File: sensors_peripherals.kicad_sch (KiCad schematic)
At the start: 17 parts, among them J2 Conn_01x14, J4 Micro_SD_Card_Det1, J5 Conn_01x14, J6 Conn_01x02, U3 W25Q128JVS, U6 ICM-42688-P

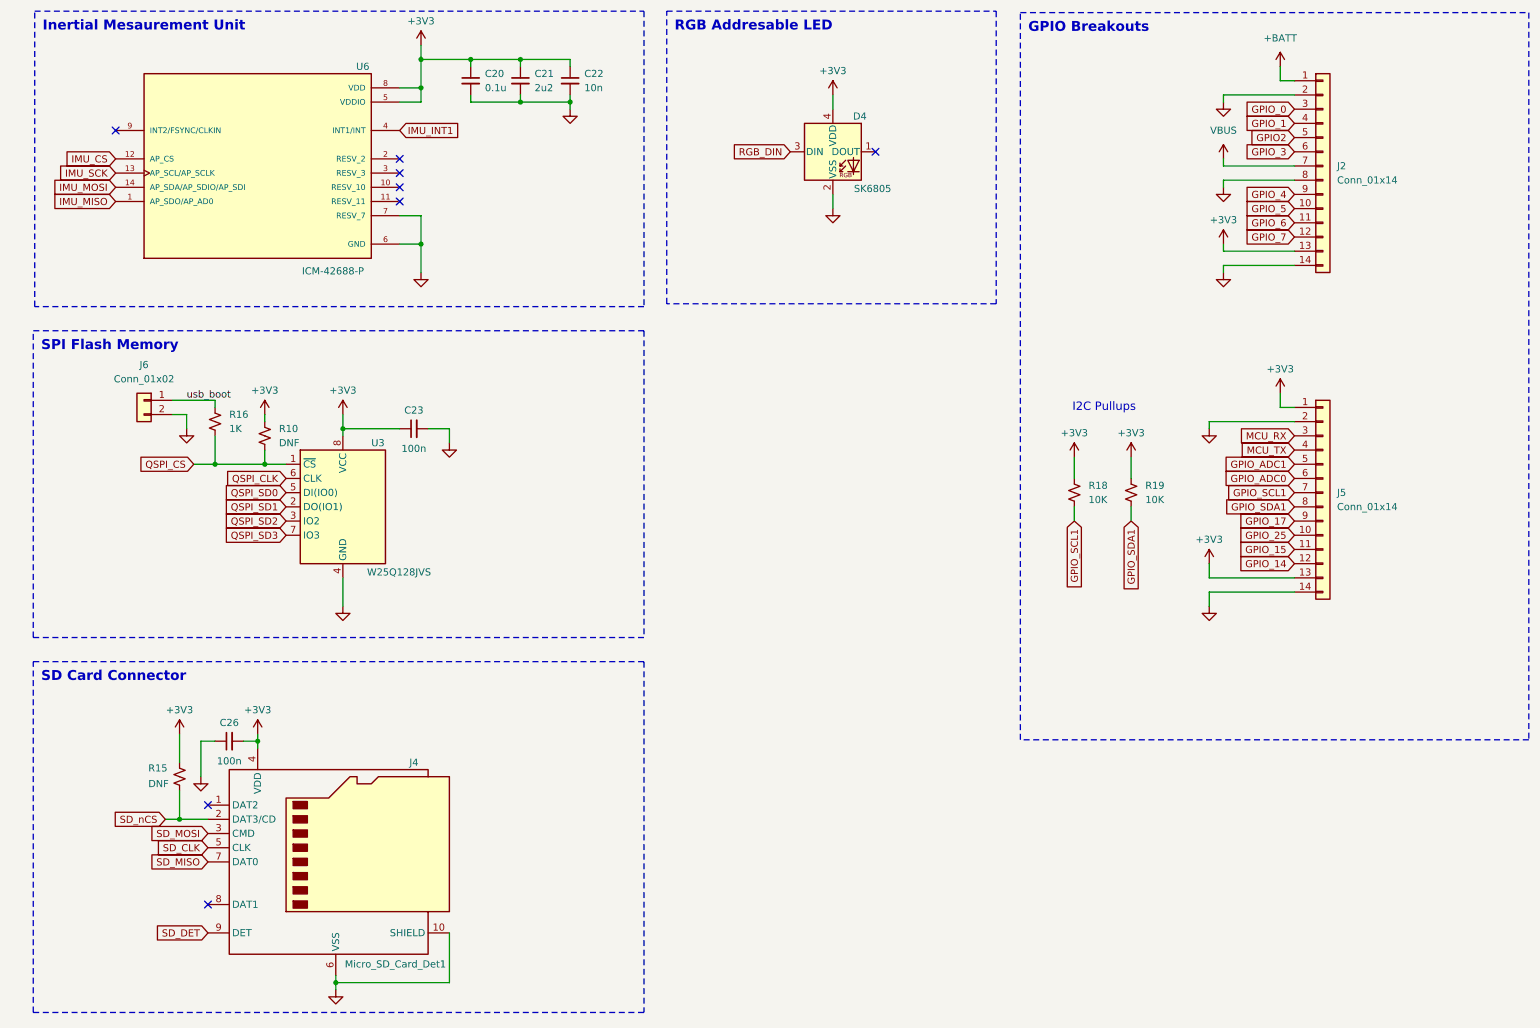
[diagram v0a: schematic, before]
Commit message: Added a bootloader button and made some other QOL changes... mostly aesthetic.
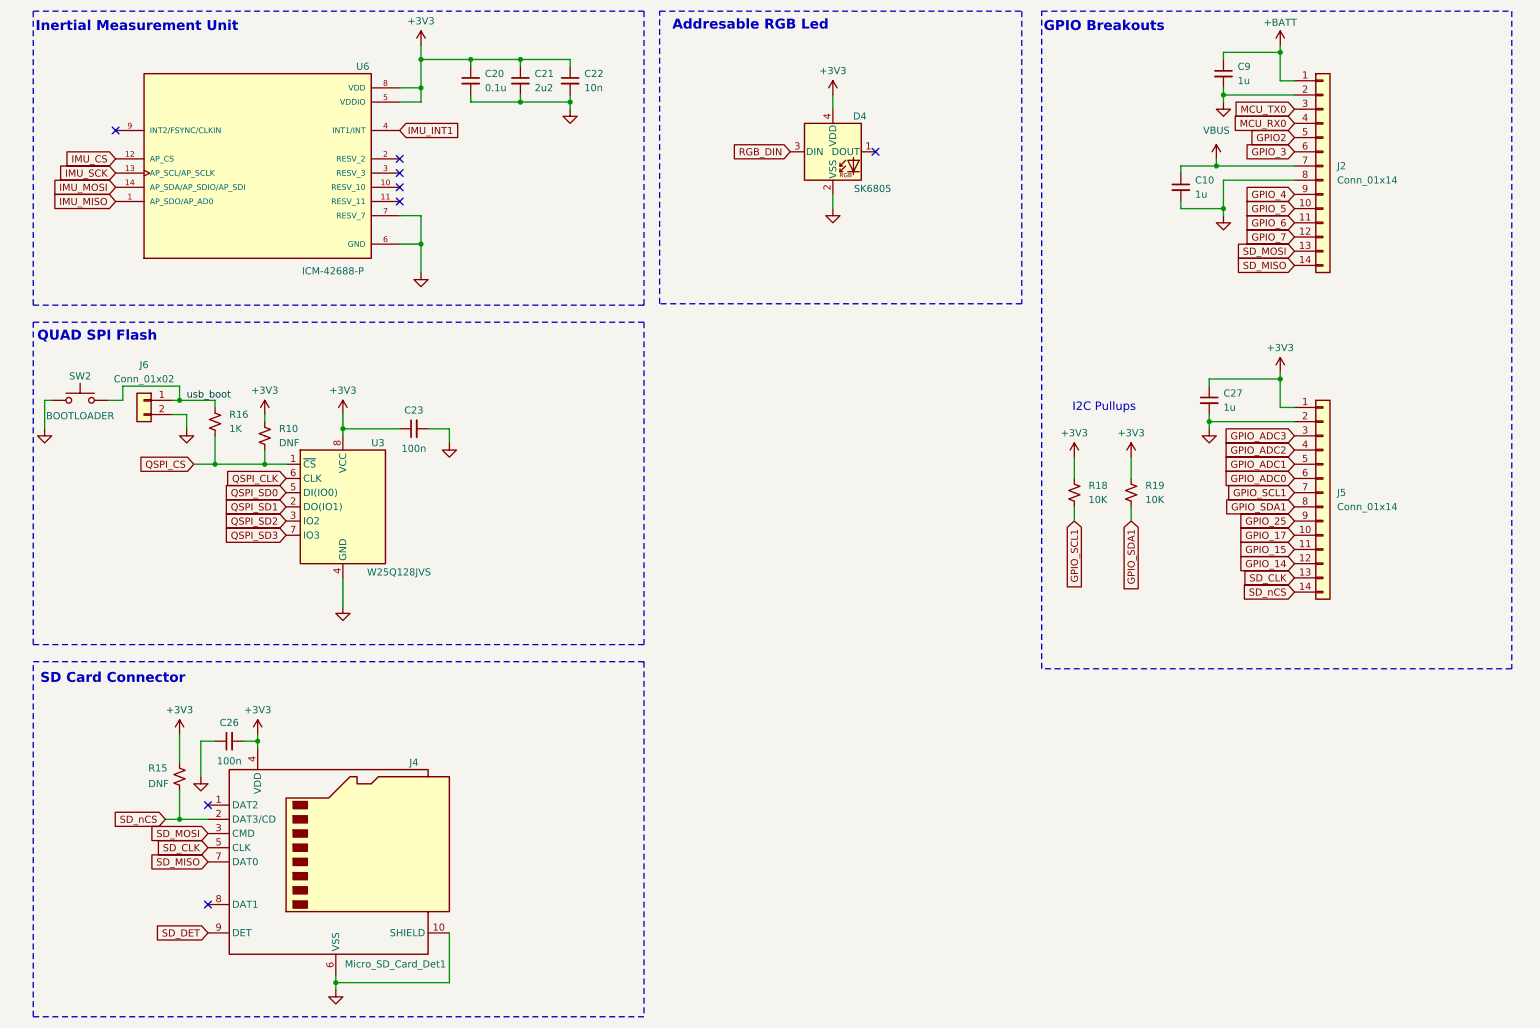
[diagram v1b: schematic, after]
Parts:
- added C10, C27, C9: 1u, Capacitor_SMD:C_0402_1005Metric, symbol Device:C_Small
- added SW2: BOOTLOADER, Button_Switch_SMD:SW_SPST_PTS647_Sx38, symbol Switch:SW_Push
- C26: footprint Capacitor_SMD:C_0201_0603Metric -> Capacitor_SMD:C_0805_2012Metric_Pad1.18x1.45mm_HandSolder
- R15: footprint Resistor_SMD:R_0805_2012Metric -> Resistor_SMD:R_0805_2012Metric_Pad1.20x1.40mm_HandSolder
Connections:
- net +3V3: now also C27.1; no longer J2.13 (Pin_13), J5.13 (Pin_13)
- net +BATT: now also C9.1
- net GND: now also C10.2, C27.2, C9.2, SW2.1; no longer J2.14 (Pin_14), J5.14 (Pin_14)
- net GPIO_17: now also J5.10 (Pin_10); no longer J5.9 (Pin_9)
- net GPIO_25: now also J5.9 (Pin_9); no longer J5.10 (Pin_10)
- net SD_CLK: now also J5.13 (Pin_13)
- net SD_MISO: now also J2.14 (Pin_14)
- net SD_MOSI: now also J2.13 (Pin_13)
- net SD_nCS: now also J5.14 (Pin_14)
- net VBUS: now also C10.1
- net usb_boot: now also SW2.2
- net GPIO_0 renamed MCU_TX0
- net GPIO_1 renamed MCU_RX0
- net MCU_RX renamed GPIO_ADC3
- net MCU_TX renamed GPIO_ADC2
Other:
- note added: "Addresable RGB Led"
- note added: "GPIO Breakouts"
- note added: "Inertial Measurement Unit"
- note added: "QUAD SPI Flash"
- note added: "SD Card Connector"

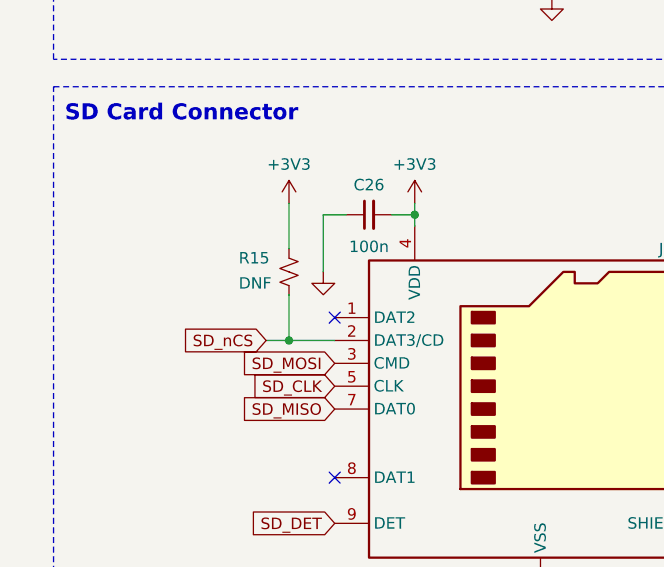
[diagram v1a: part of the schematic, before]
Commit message: removed the DNF silkscreen for the SD Card connector's CS pin pullup resistor
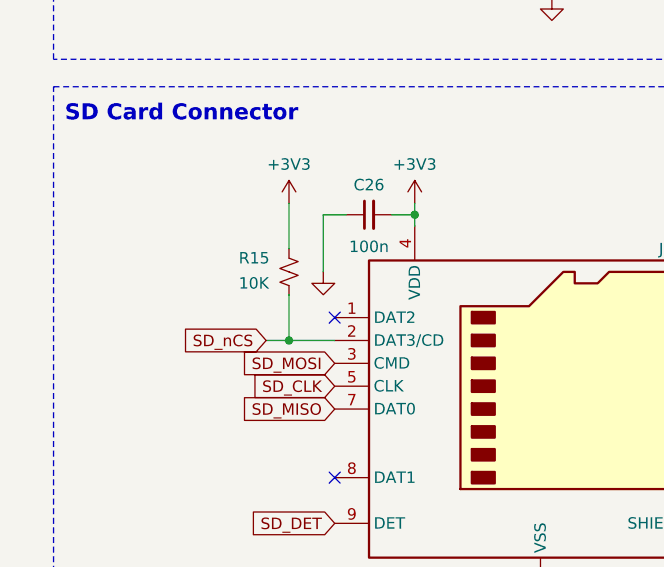
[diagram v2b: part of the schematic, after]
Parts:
- R15: value DNF -> 10K
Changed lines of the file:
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@@
 			)
 		)
-		(property "Value" "DNF"
+		(property "Value" "10K"
 			(at 36.322 153.67 0)
 			(effects
